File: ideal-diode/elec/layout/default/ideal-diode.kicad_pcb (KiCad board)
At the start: 2 copper layers, 225.7 x 100.8 mm, 0 parts

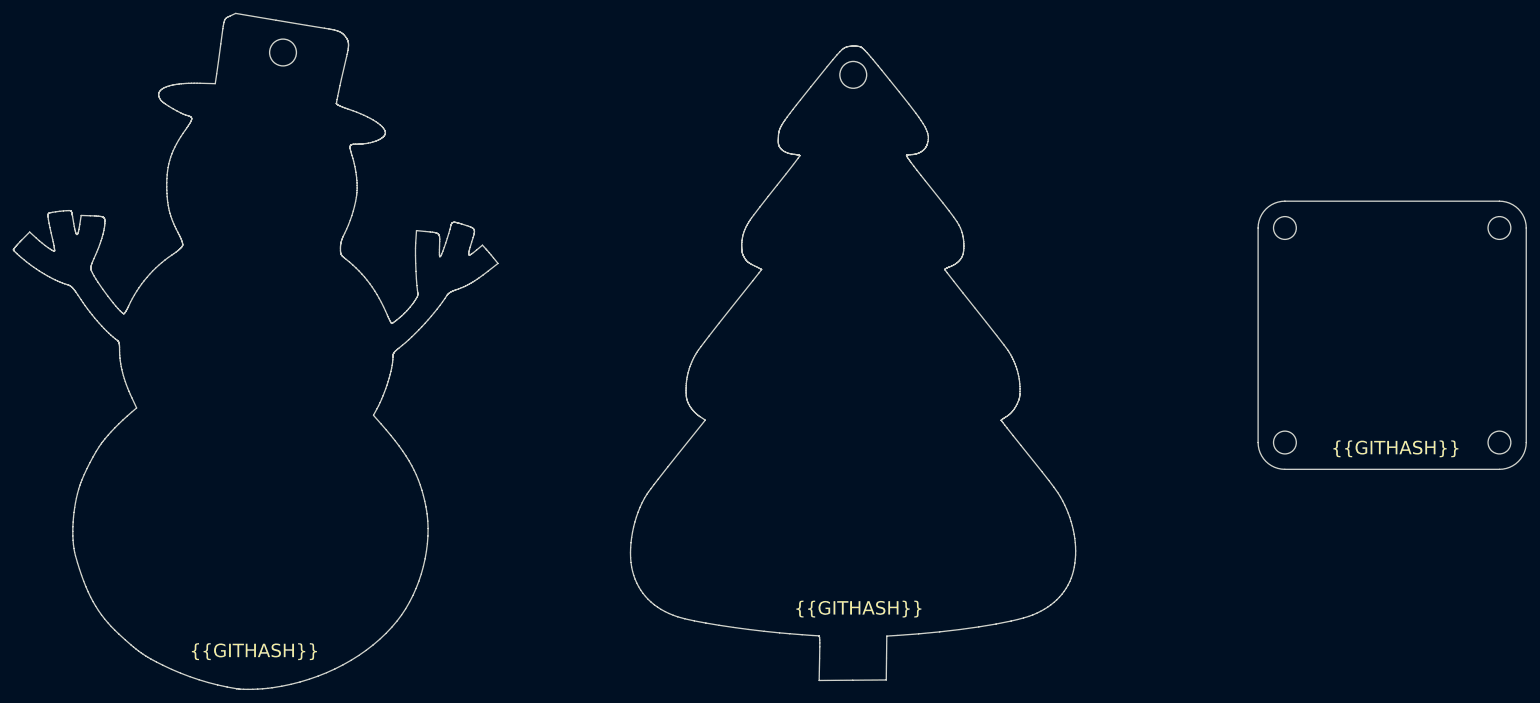
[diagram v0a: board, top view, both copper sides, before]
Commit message: added pcb layout for ideal-diode
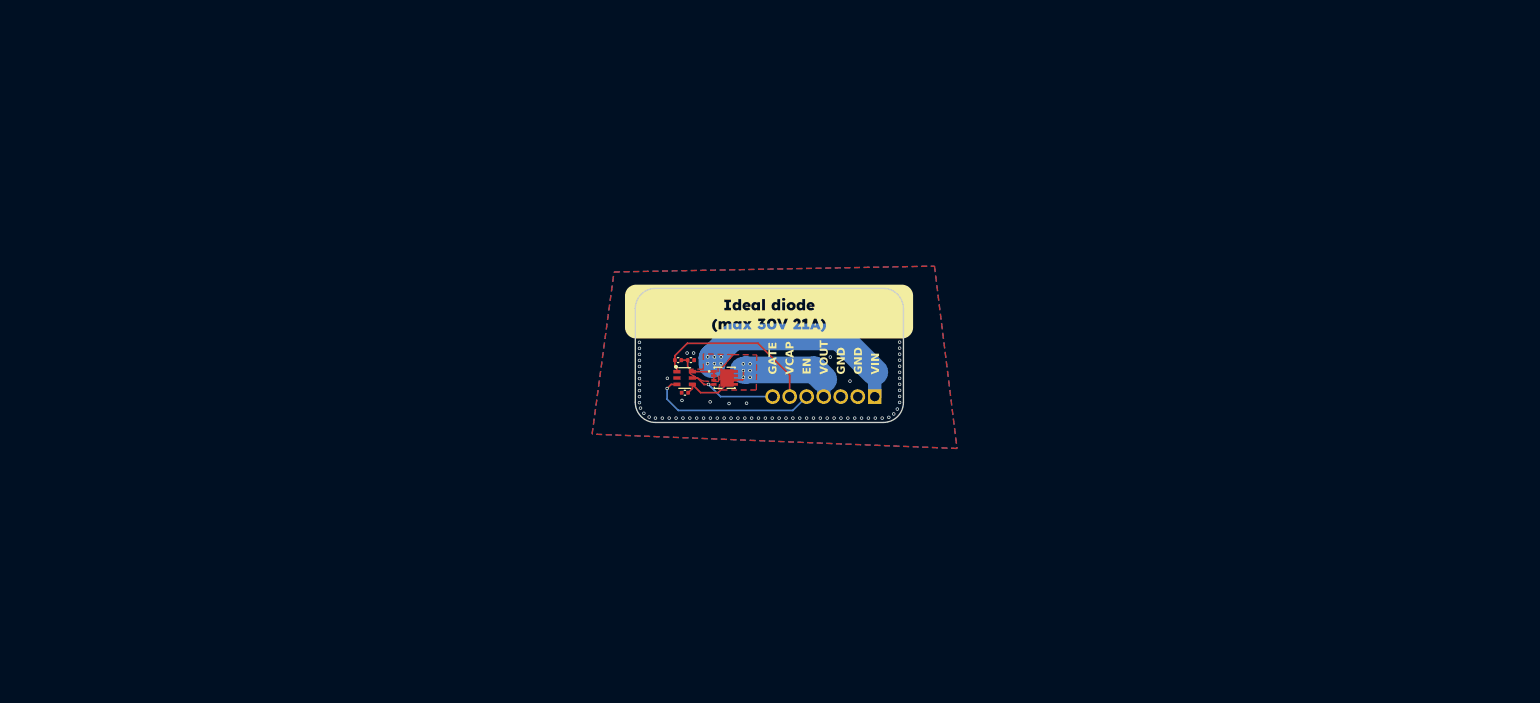
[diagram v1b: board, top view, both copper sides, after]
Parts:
- added C1: 50V 22nF X7R ±10% 0402 Multilayer Ceramic Capacitors MLCC -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, lib:C0402, F.Cu at (137.0, 101.5)
- added C2: 16V 100nF X7R ±10% 0402 Multilayer Ceramic Capacitors MLCC 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, lib:C0402, F.Cu at (135.1, 101.5)
- added C3: 16V 100nF X7R ±10% 0402 Multilayer Ceramic Capacitors MLCC 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, lib:C0402, F.Cu at (136.1, 106.4)
- added Q1: , lib:PDFN-8_L3.2-W3.0-P0.65-LS3.3-BL-1, F.Cu at (142.0, 104.2)
- added U1: , lib:SOT-23-6_L2.9-W1.6-P0.95-LS2.8-BL, F.Cu at (136.1, 104.2)
- added U2: , lib:CONN-TH_XY308-2.54-7P, F.Cu at (156.8, 106.9)
- added U3: , lib:MountingHole_3.2mm_M3, F.Cu at (133.0, 95.0)
- added U4: , lib:MountingHole_3.2mm_M3, F.Cu at (164.5, 95.0)
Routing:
- net anode: track 0.00 -> 39.9 mm, vias 0 -> 6
- net cathode: track 0.00 -> 27.7 mm, vias 0 -> 6
- net en: track 0.00 -> 25.7 mm, vias 0 -> 1
- net vcap: track 0.00 -> 25.6 mm
- net gate: track 0.00 -> 13.9 mm, vias 0 -> 1
- net gnd: vias 0 -> 153
- added copper zone on F.Cu, net anode
- added copper zone on F.Cu, net cathode
- added copper zone on B.Cu, net gnd
- added copper zone on F.Cu, net gnd
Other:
- board size 225.7 x 100.8 mm -> 40 x 20 mm
- board text added: "EN"
- board text added: "GATE"
- board text added: "GND"
- board text added: "Source files:"
- board text added: "VCAP"
- board text added: "VIN"
- board text added: "VOUT"
- board text added: "bit.ly/3VUwVZU"
- board text added: "designed by glowingkitty"
